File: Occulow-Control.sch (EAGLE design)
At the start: 1 part

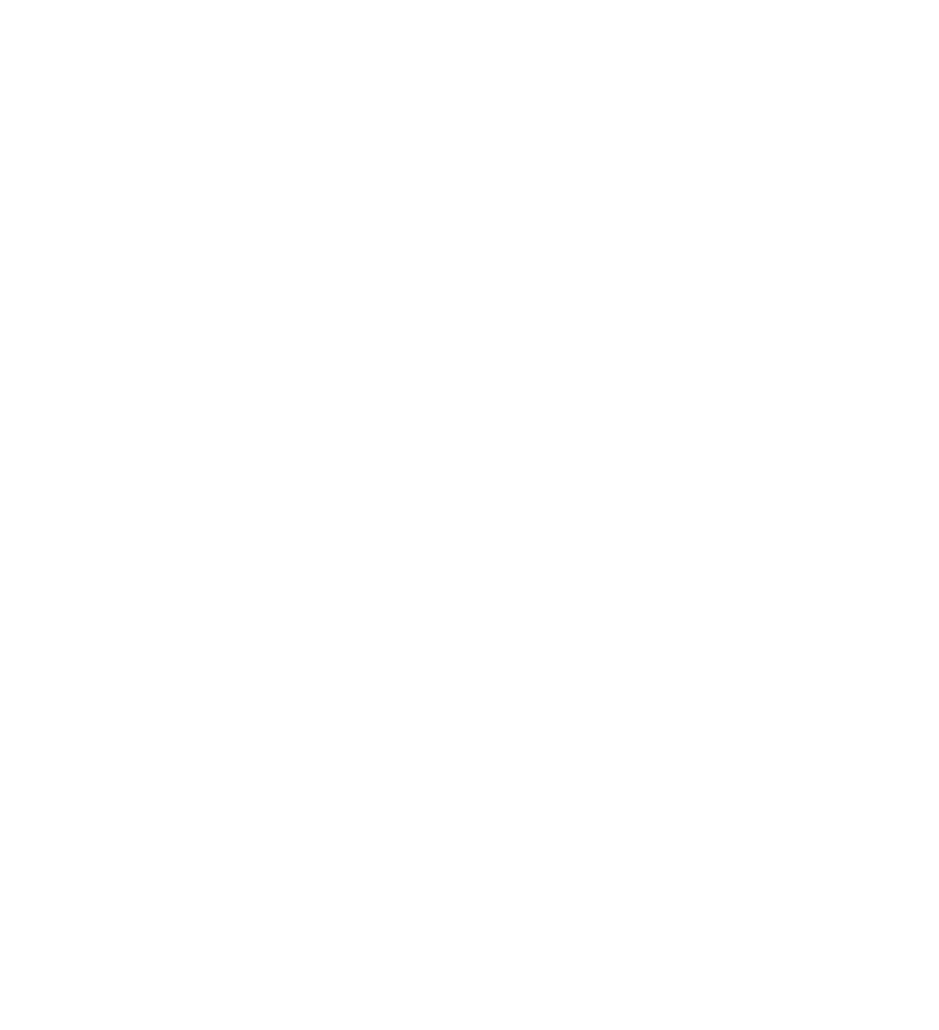
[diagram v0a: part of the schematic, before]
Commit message: Updated sam lbr to ease schematic dev
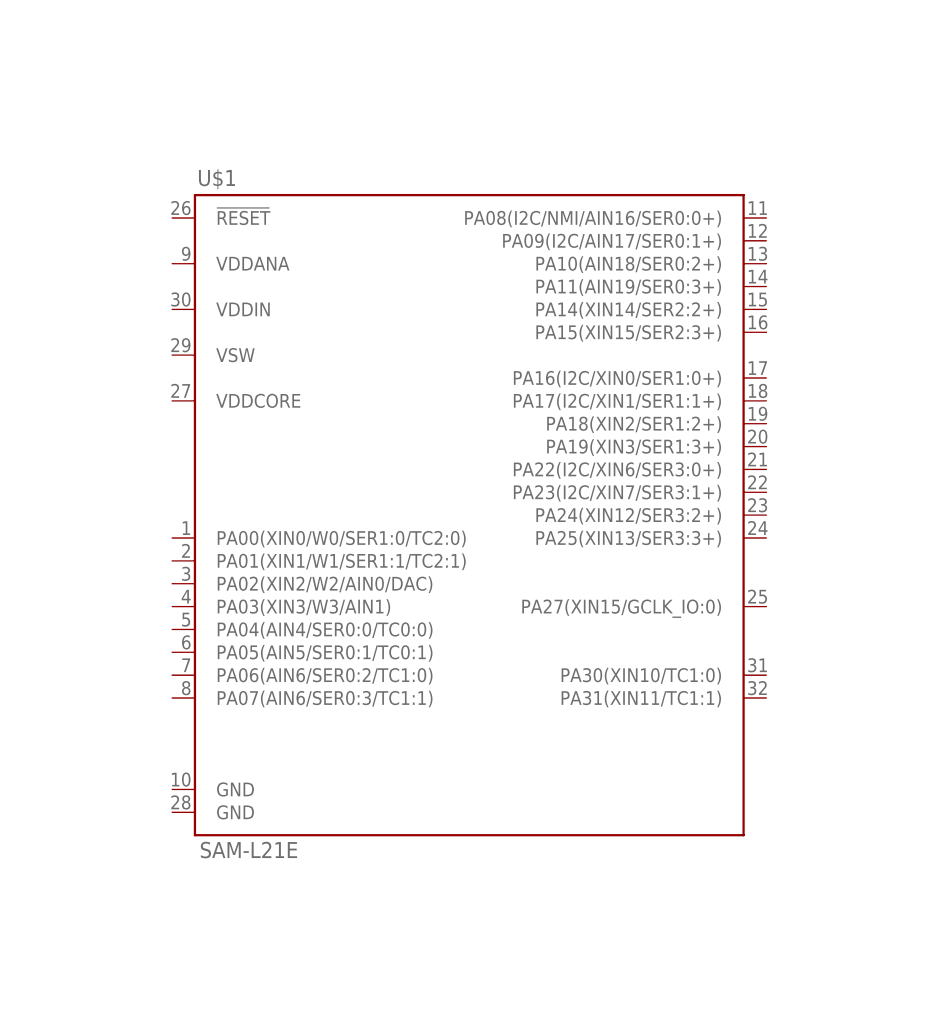
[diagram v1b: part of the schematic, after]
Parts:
- added U$1: SAM-L21E, SAML21-TQFP32:SAM-L21E
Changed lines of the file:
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@@
 <parts>
 <part name="FRAME1" library="SparkFun-Aesthetics" deviceset="FRAME-LETTER" device="NO_PACKAGE"/>
+<part name="U$1" library="SAML21-TQFP32" deviceset="SAM-L21E" device=""/>
 </parts>
 <sheets>
@@
 <instance part="FRAME1" gate="G$1" x="0" y="0"/>
 <instance part="FRAME1" gate="V" x="147.32" y="0"/>
+<instance part="U$1" gate="G$1" x="121.92" y="106.68"/>
 </instances>
 <busses>

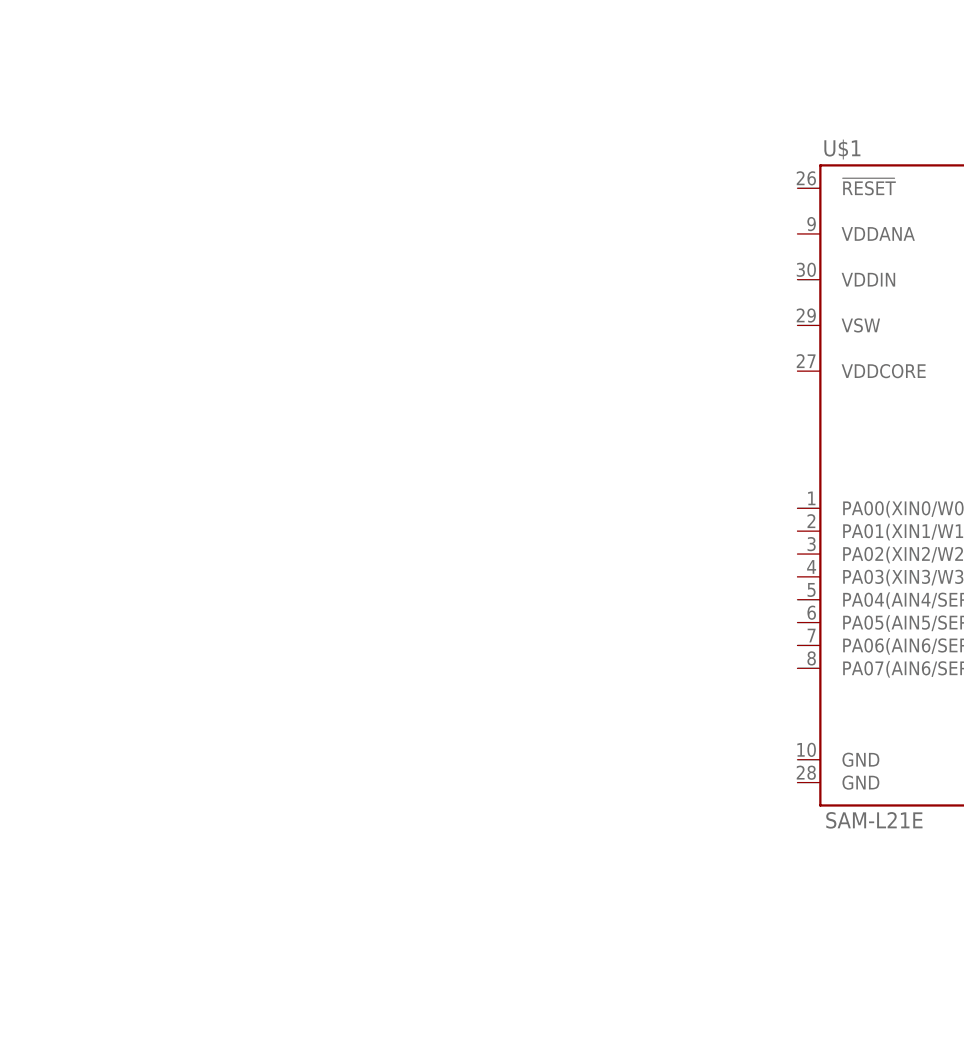
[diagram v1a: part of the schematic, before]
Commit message: Start of power circuit for sam chip
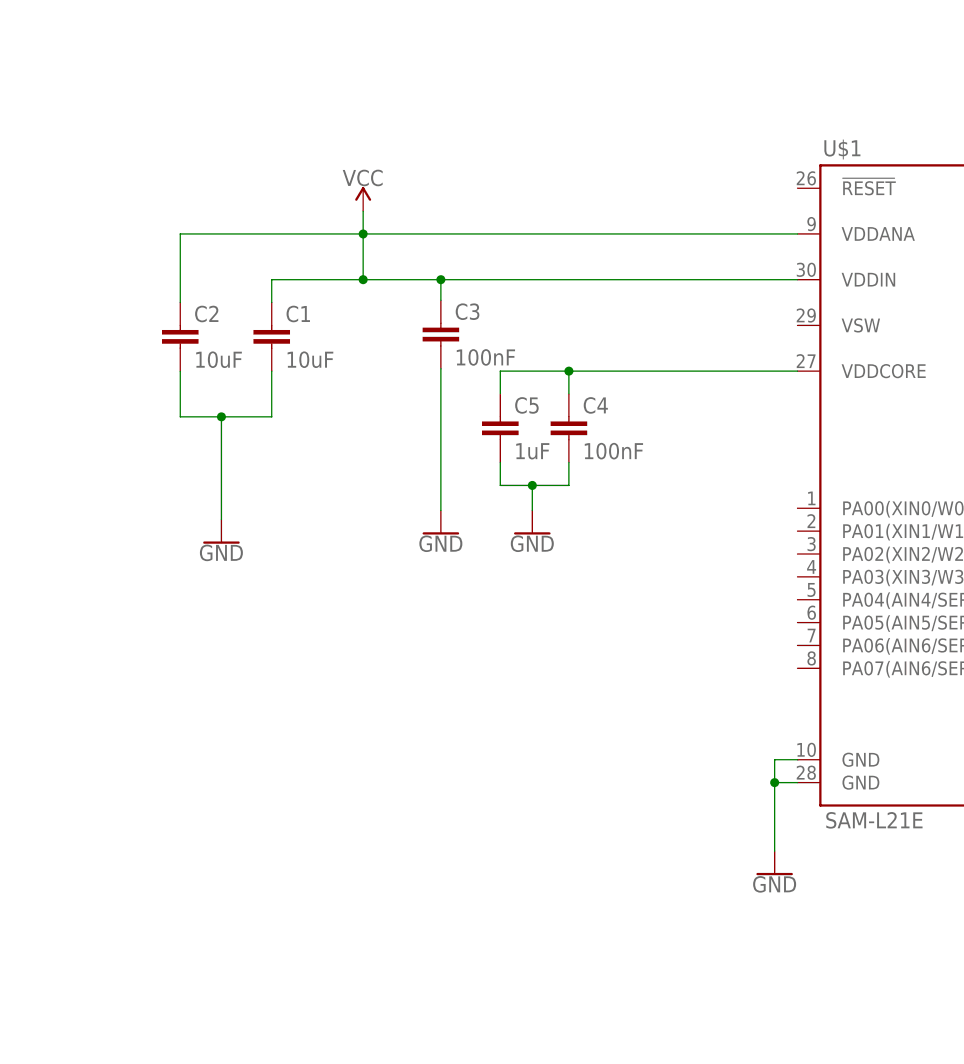
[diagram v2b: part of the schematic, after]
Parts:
- added C1, C2: 10uF, rcl:C-EUC1206
- added C3, C4: 100nF, rcl:C-EUC1206
- added C5: 1uF, rcl:C-EUC1206
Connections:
- new net GND: C1.2, C2.2, C3.2, C4.2, C5.2, U$1.GND@1, U$1.GND@2
- new net N$1: C4.1, C5.1, U$1.VDDCORE
- new net VCC: C1.1, C2.1, C3.1, U$1.VDDANA, U$1.VDDIN
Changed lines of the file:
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@@
 <part name="FRAME1" library="SparkFun-Aesthetics" deviceset="FRAME-LETTER" device="NO_PACKAGE"/>
 <part name="U$1" library="SAML21-TQFP32" deviceset="SAM-L21E" device=""/>
+<part name="C1" library="rcl" deviceset="C-EU" device="C1206" value="10uF"/>
+<part name="GND1" library="SparkFun-PowerSymbols" deviceset="GND" device=""/>
+<part name="SUPPLY1" library="SparkFun-PowerSymbols" deviceset="VCC" device=""/>
+<part name="C2" library="rcl" deviceset="C-EU" device="C1206" value="10uF"/>
+<part name="C3" library="rcl" deviceset="C-EU" device="C1206" value="100nF"/>
+<part name="C4" library="rcl" deviceset="C-EU" device="C1206" value="100nF"/>
+<part name="C5" library="rcl" deviceset="C-EU" device="C1206" value="1uF"/>
+<part name="GND4" library="SparkFun-PowerSymbols" deviceset="GND" device=""/>
+<part name="GND2" library="SparkFun-PowerSymbols" deviceset="GND" device=""/>
+<part name="GND3" library="SparkFun-PowerSymbols" deviceset="GND" device=""/>
 </parts>
 <sheets>
@@
 <instance part="FRAME1" gate="V" x="147.32" y="0"/>
 <instance part="U$1" gate="G$1" x="121.92" y="106.68"/>
+<instance part="C1" gate="G$1" x="30.48" y="124.46"/>
+<instance part="GND1" gate="1" x="86.36" y="63.5"/>
+<instance part="SUPPLY1" gate="G$1" x="40.64" y="137.16"/>
+<instance part="C2" gate="G$1" x="20.32" y="124.46"/>
+<instance part="C3" gate="G$1" x="49.276" y="124.714"/>
+<instance part="C4" gate="G$1" x="63.5" y="114.3"/>
+<instance part="C5" gate="G$1" x="55.88" y="114.3"/>
+<instance part="GND4" gate="1" x="59.436" y="101.346"/>
+<instance part="GND2" gate="1" x="24.892" y="100.33"/>
+<instance part="GND3" gate="1" x="49.276" y="101.346"/>
 </instances>
 <busses>
 </busses>
 <nets>
+<net name="GND" class="0">
+<segment>
+<pinref part="U$1" gate="G$1" pin="GND@1"/>
+<wire x1="88.9" y1="76.2" x2="86.36" y2="76.2" width="0.1524" layer="91"/>
+<wire x1="86.36" y1="76.2" x2="86.36" y2="73.66" width="0.1524" layer="91"/>
+<pinref part="U$1" gate="G$1" pin="GND@2"/>
+<wire x1="86.36" y1="73.66" x2="86.36" y2="66.04" width="0.1524" layer="91"/>
+<wire x1="88.9" y1="73.66" x2="86.36" y2="73.66" width="0.1524" layer="91"/>
+<junction x="86.36" y="73.66"/>
+<pinref part="GND1" gate="1" pin="GND"/>
+</segment>
+<segment>
+<pinref part="C5" gate="G$1" pin="2"/>
+<wire x1="55.88" y1="109.22" x2="55.88" y2="106.68" width="0.1524" layer="91"/>
+<pinref part="C4" gate="G$1" pin="2"/>
+<wire x1="63.5" y1="109.22" x2="63.5" y2="106.68" width="0.1524" layer="91"/>
+<wire x1="63.5" y1="106.68" x2="59.436" y2="106.68" width="0.1524" layer="91"/>
+<pinref part="GND4" gate="1" pin="GND"/>
+<wire x1="59.436" y1="106.68" x2="55.88" y2="106.68" width="0.1524" layer="91"/>
+<wire x1="59.436" y1="103.886" x2="59.436" y2="106.68" width="0.1524" layer="91"/>
+<junction x="59.436" y="106.68"/>
+</segment>
+<segment>
+<pinref part="C1" gate="G$1" pin="2"/>
+<wire x1="30.48" y1="119.38" x2="30.48" y2="114.3" width="0.1524" layer="91"/>
+<pinref part="C2" gate="G$1" pin="2"/>
+<wire x1="20.32" y1="119.38" x2="20.32" y2="114.3" width="0.1524" layer="91"/>
+<wire x1="30.48" y1="114.3" x2="24.892" y2="114.3" width="0.1524" layer="91"/>
+<pinref part="GND2" gate="1" pin="GND"/>
+<wire x1="24.892" y1="114.3" x2="20.32" y2="114.3" width="0.1524" layer="91"/>
+<wire x1="24.892" y1="102.87" x2="24.892" y2="114.3" width="0.1524" layer="91"/>
+<junction x="24.892" y="114.3"/>
+</segment>
+<segment>
+<pinref part="GND3" gate="1" pin="GND"/>
+<pinref part="C3" gate="G$1" pin="2"/>
+<wire x1="49.276" y1="103.886" x2="49.276" y2="119.634" width="0.1524" layer="91"/>
+</segment>
+</net>
+<net name="VCC" class="0">
+<segment>
+<pinref part="U$1" gate="G$1" pin="VDDIN"/>
+<pinref part="C1" gate="G$1" pin="1"/>
+<wire x1="88.9" y1="129.54" x2="49.276" y2="129.54" width="0.1524" layer="91"/>
+<wire x1="49.276" y1="129.54" x2="40.64" y2="129.54" width="0.1524" layer="91"/>
+<wire x1="40.64" y1="129.54" x2="30.48" y2="129.54" width="0.1524" layer="91"/>
+<wire x1="30.48" y1="129.54" x2="30.48" y2="127" width="0.1524" layer="91"/>
+<pinref part="SUPPLY1" gate="G$1" pin="VCC"/>
+<wire x1="40.64" y1="137.16" x2="40.64" y2="134.62" width="0.1524" layer="91"/>
+<junction x="40.64" y="129.54"/>
+<pinref part="U$1" gate="G$1" pin="VDDANA"/>
+<wire x1="40.64" y1="134.62" x2="40.64" y2="129.54" width="0.1524" layer="91"/>
+<wire x1="88.9" y1="134.62" x2="40.64" y2="134.62" width="0.1524" layer="91"/>
+<junction x="40.64" y="134.62"/>
+<pinref part="C2" gate="G$1" pin="1"/>
+<wire x1="40.64" y1="134.62" x2="20.32" y2="134.62" width="0.1524" layer="91"/>
+<wire x1="20.32" y1="134.62" x2="20.32" y2="127" width="0.1524" layer="91"/>
+<pinref part="C3" gate="G$1" pin="1"/>
+<wire x1="49.276" y1="127.254" x2="49.276" y2="129.54" width="0.1524" layer="91"/>
+<junction x="49.276" y="129.54"/>
+</segment>
+</net>
+<net name="N$1" class="0">
+<segment>
+<pinref part="U$1" gate="G$1" pin="VDDCORE"/>
+<pinref part="C4" gate="G$1" pin="1"/>
+<wire x1="88.9" y1="119.38" x2="63.5" y2="119.38" width="0.1524" layer="91"/>
+<wire x1="63.5" y1="119.38" x2="63.5" y2="116.84" width="0.1524" layer="91"/>
+<pinref part="C5" gate="G$1" pin="1"/>
+<wire x1="63.5" y1="119.38" x2="55.88" y2="119.38" width="0.1524" layer="91"/>
+<wire x1="55.88" y1="119.38" x2="55.88" y2="116.84" width="0.1524" layer="91"/>
+<junction x="63.5" y="119.38"/>
+</segment>
+</net>
 </nets>
 </sheet>

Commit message: Port lora module
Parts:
- added C6: 10uF, rcl:C-EUC1206
- added U$2: RN2903, RN2903:RN2903
- added U$3: SMA-JACKFEMALE, SMA-JACK:SMA-JACKFEMALE
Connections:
- new net LR_CTS: U$2.UART_CTS
- new net LR_RST_N: U$2.RESET_N
- new net LR_RTS: U$2.UART_RTS
- new net LR_RX: U$2.UART_RX
- new net LR_TX: U$2.UART_TX
- new net LR_VCC: C6.1, U$2.VDD1, U$2.VDD2
- new net RF: U$2.RF, U$3.RF
- net GND: now also C6.2, U$2.GND1, U$2.GND10, U$2.GND11, U$2.GND12, U$2.GND13, U$2.GND2, U$2.GND3, U$2.GND4, U$2.GND5, U$2.GND6, U$2.GND7, U$2.GND8, U$2.GND9, U$3.GND1, U$3.GND2, U$3.GND3, U$3.GND4
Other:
- moved on the sheet: C1, C2, C3, C4, C5, U$1

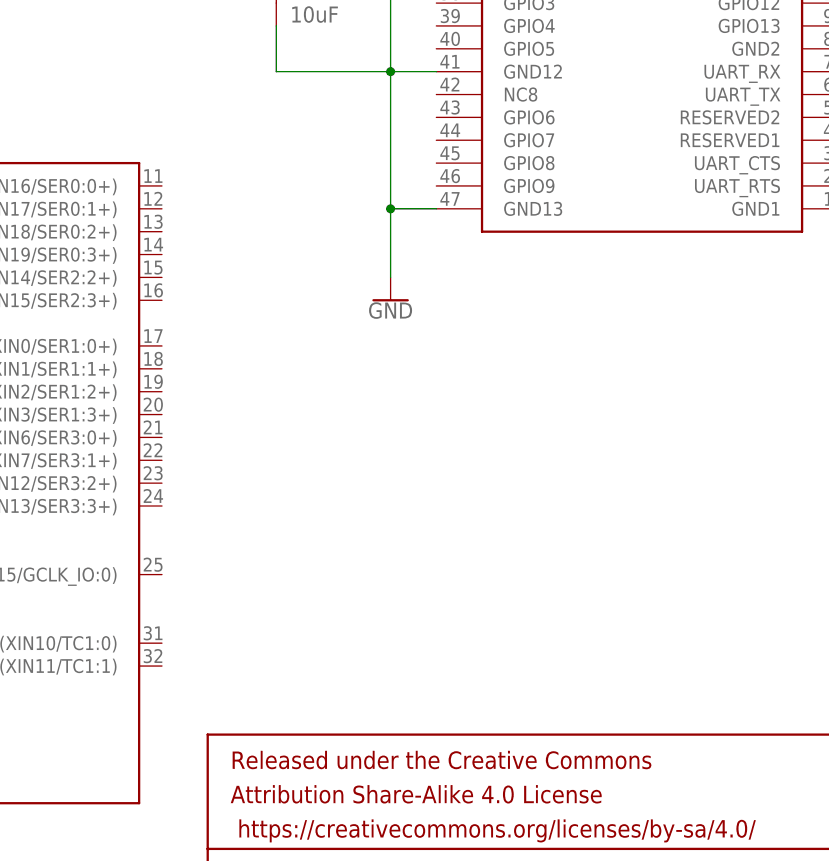
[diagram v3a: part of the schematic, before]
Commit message: Lora and SAM chip integrated
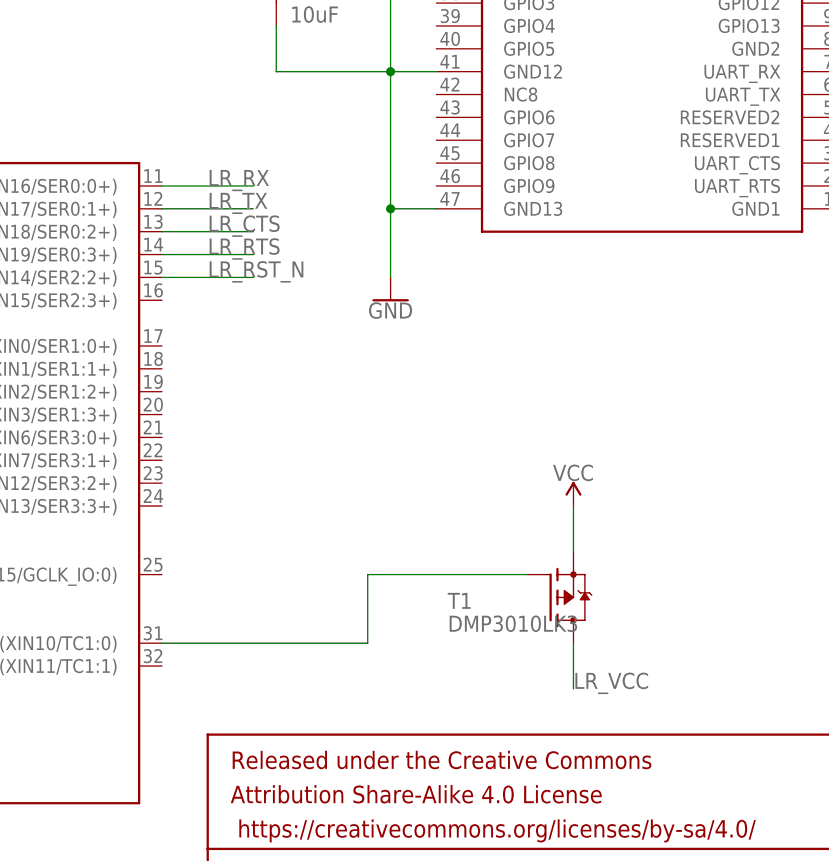
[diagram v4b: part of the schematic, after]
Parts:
- added T1: DMP3010LK3, transistor-fet:SPD30P06PTO252
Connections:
- new net N$2: T1.G, U$1.PA30(XIN10/TC1:0)
- net LR_CTS: now also U$1.PA10(AIN18/SER0:2+)
- net LR_RST_N: now also U$1.PA14(XIN14/SER2:2+)
- net LR_RTS: now also U$1.PA11(AIN19/SER0:3+)
- net LR_RX: now also U$1.PA08(I2C/NMI/AIN16/SER0:0+)
- net LR_TX: now also U$1.PA09(I2C/AIN17/SER0:1+)
- net LR_VCC: now also T1.D
- net VCC: now also T1.S
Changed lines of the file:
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@@
 <part name="GND7" library="SparkFun-PowerSymbols" deviceset="GND" device=""/>
 <part name="GND8" library="SparkFun-PowerSymbols" deviceset="GND" device=""/>
+<part name="T1" library="transistor-fet" deviceset="SPD30P06P" device="TO252" value="DMP3010LK3"/>
+<part name="SUPPLY2" library="SparkFun-PowerSymbols" deviceset="VCC" device=""/>
 </parts>
 <sheets>
@@
 <instance part="GND7" gate="1" x="210.82" y="147.32"/>
 <instance part="GND8" gate="1" x="215.9" y="160.02"/>
+<instance part="T1" gate="G$1" x="185.42" y="50.8"/>
+<instance part="SUPPLY2" gate="G$1" x="187.96" y="60.96"/>
 </instances>
 <busses>
@@
 <junction x="36.576" y="86.36"/>
 </segment>
+<segment>
+<pinref part="SUPPLY2" gate="G$1" pin="VCC"/>
+<pinref part="T1" gate="G$1" pin="S"/>
+<wire x1="187.96" y1="60.96" x2="187.96" y2="55.88" width="0.1524" layer="91"/>
+</segment>
 </net>
 <net name="N$1" class="0">
@@
 <label x="228.6" y="109.22" size="1.778" layer="95"/>
 </segment>
+<segment>
+<pinref part="U$1" gate="G$1" pin="PA08(I2C/NMI/AIN16/SER0:0+)"/>
+<wire x1="142.24" y1="96.52" x2="152.4" y2="96.52" width="0.1524" layer="91"/>
+<label x="147.32" y="96.52" size="1.778" layer="95"/>
+</segment>
 </net>
 <net name="LR_TX" class="0">
@@
 <label x="228.6" y="106.68" size="1.778" layer="95"/>
 </segment>
+<segment>
+<pinref part="U$1" gate="G$1" pin="PA09(I2C/AIN17/SER0:1+)"/>
+<wire x1="142.24" y1="93.98" x2="152.4" y2="93.98" width="0.1524" layer="91"/>
+<label x="147.32" y="93.98" size="1.778" layer="95"/>
+</segment>
 </net>
 <net name="LR_CTS" class="0">
@@
 <label x="228.6" y="99.06" size="1.778" layer="95"/>
 </segment>
+<segment>
+<pinref part="U$1" gate="G$1" pin="PA10(AIN18/SER0:2+)"/>
+<wire x1="142.24" y1="91.44" x2="152.4" y2="91.44" width="0.1524" layer="91"/>
+<label x="147.32" y="91.44" size="1.778" layer="95"/>
+</segment>
 </net>
 <net name="LR_RTS" class="0">
@@
 <wire x1="218.44" y1="96.52" x2="238.76" y2="96.52" width="0.1524" layer="91"/>
 <label x="228.6" y="96.52" size="1.778" layer="95"/>
+</segment>
+<segment>
+<pinref part="U$1" gate="G$1" pin="PA11(AIN19/SER0:3+)"/>
+<wire x1="142.24" y1="88.9" x2="152.4" y2="88.9" width="0.1524" layer="91"/>
+<label x="147.32" y="88.9" size="1.778" layer="95"/>
 </segment>
 </net>
@@
 <label x="154.94" y="152.4" size="1.778" layer="95"/>
 </segment>
+<segment>
+<pinref part="T1" gate="G$1" pin="D"/>
+<wire x1="187.96" y1="45.72" x2="187.96" y2="40.64" width="0.1524" layer="91"/>
+<label x="187.96" y="40.64" size="1.778" layer="95"/>
+</segment>
 </net>
 <net name="LR_RST_N" class="0">
@@
 <label x="157.48" y="132.08" size="1.778" layer="95"/>
 </segment>
-</net>
+<segment>
+<pinref part="U$1" gate="G$1" pin="PA14(XIN14/SER2:2+)"/>
+<wire x1="142.24" y1="86.36" x2="152.4" y2="86.36" width="0.1524" layer="91"/>
+<label x="147.32" y="86.36" size="1.778" layer="95"/>
+</segment>
+</net>
+<net name="N$2" class="0">
+<segment>
+<pinref part="U$1" gate="G$1" pin="PA30(XIN10/TC1:0)"/>
+<wire x1="142.24" y1="45.72" x2="165.1" y2="45.72" width="0.1524" layer="91"/>
+<wire x1="165.1" y1="45.72" x2="165.1" y2="53.34" width="0.1524" layer="91"/>
+<pinref part="T1" gate="G$1" pin="G"/>
+<wire x1="165.1" y1="53.34" x2="182.88" y2="53.34" width="0.1524" layer="91"/>
+</segment>
+</net>
